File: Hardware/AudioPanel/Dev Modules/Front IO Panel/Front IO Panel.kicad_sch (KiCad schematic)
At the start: 78 parts, among them J101 Screw_Terminal_01x02, J102 2.54mm, J103 JST-PH UART/I2C, J104 2.54mm, U101 AZ1117-5.0, U102 INA219AxDCN, U103 AP3012, U106 NXB0106BQX, U109 QTPy SAMD21, U110 USBLC6-2SC6, U111 USBLC6-2SC6

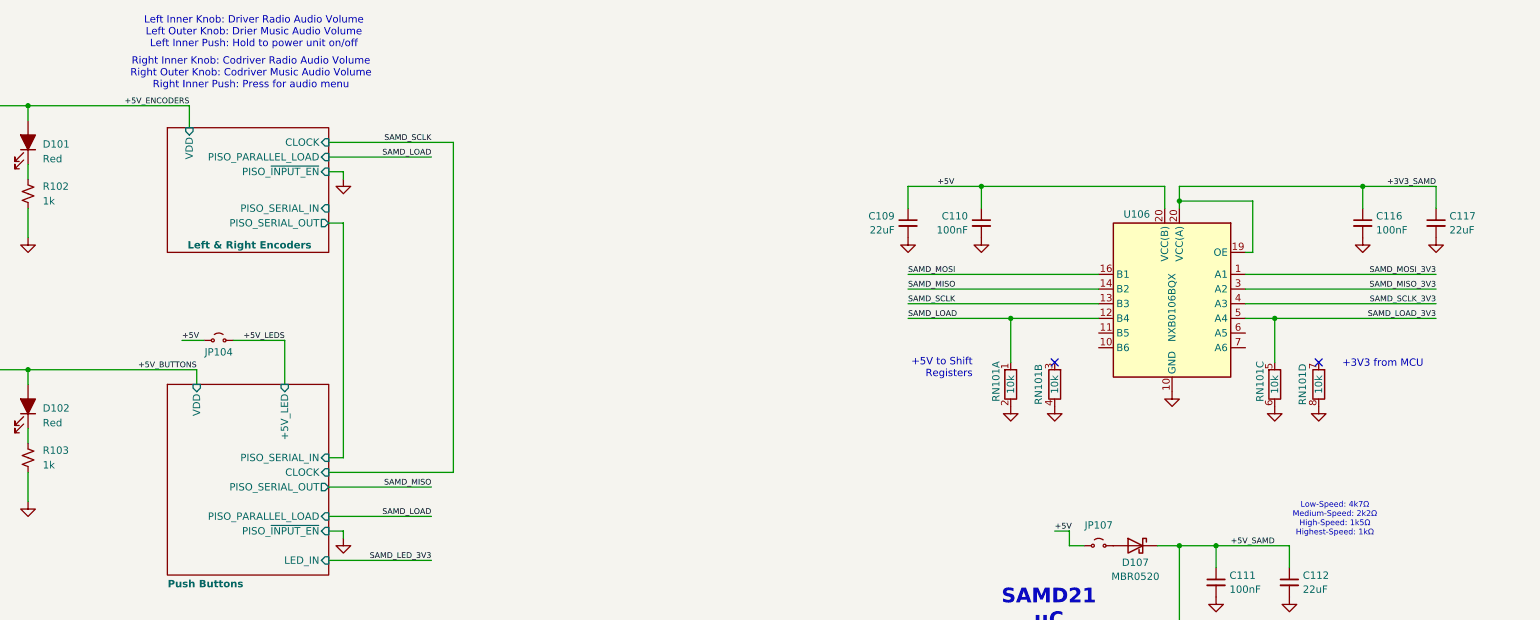
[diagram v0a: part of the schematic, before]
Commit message: Re-organized pull up/dwn resistors in schematic
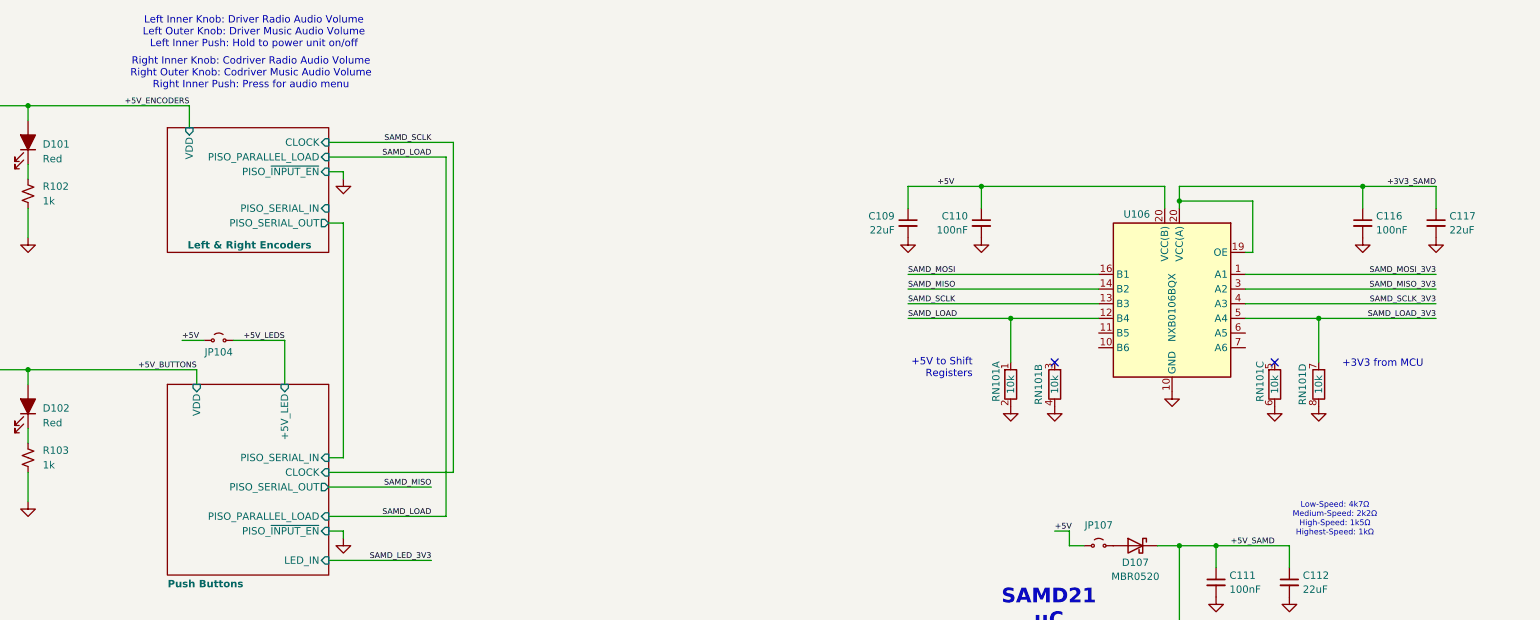
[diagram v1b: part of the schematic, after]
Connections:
- net SAMD_LOAD_3V3: now also RN101.7; no longer RN101.5
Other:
- note added: "Left Inner Knob: Driver Radio Audio Volume Left Outer Knob: Driver Music Audio Volume Left Inner Push: Hold to power unit on/off"
- note removed: "Left Inner Knob: Driver Radio Audio Volume Left Outer Knob: Drier Music Audio Volume Left Inner Push: Hold to power unit on/off"
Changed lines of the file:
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@@
 		)
 	)
-	(text "Left Inner Knob: Driver Radio Audio Volume\nLeft Outer Knob: Drier Music Audio Volume\nLeft Inner Push: Hold to power unit on/off"
+	(text "Left Inner Knob: Driver Radio Audio Volume\nLeft Outer Knob: Driver Music Audio Volume\nLeft Inner Push: Hold to power unit on/off"
 		(exclude_from_sim no)
 		(at 79.756 46.99 0)
@@
 	)
 	(junction
-		(at 256.54 96.52)
-		(diameter 0)
-		(color 0 0 0 0)
-	)
-	(junction
 		(at 242.57 232.41)
 		(diameter 0)
@@
 	)
 	(junction
+		(at 264.16 96.52)
+		(diameter 0)
+		(color 0 0 0 0)
+	)
+	(junction
 		(at 240.03 135.89)
 		(diameter 0)
@@
 	)
 	(no_connect
-		(at 264.16 104.14)
+		(at 256.54 104.14)
 	)
 	(wire
@@
 	(wire
 		(pts
-			(xy 256.54 96.52) (xy 284.48 96.52)
-		)
-		(stroke
-			(width 0)
-			(type default)
-		)
-	)
-	(wire
-		(pts
 			(xy 92.71 173.99) (xy 106.68 173.99)
 		)
@@
 	(wire
 		(pts
-			(xy 251.46 96.52) (xy 256.54 96.52)
+			(xy 251.46 96.52) (xy 264.16 96.52)
 		)
 		(stroke
@@
 	(wire
 		(pts
-			(xy 256.54 96.52) (xy 256.54 104.14)
+			(xy 264.16 96.52) (xy 264.16 104.14)
 		)
 		(stroke
@@
 	(wire
 		(pts
+			(xy 264.16 96.52) (xy 284.48 96.52)
+		)
+		(stroke
+			(width 0)
+			(type default)
+		)
+	)
+	(wire
+		(pts
 			(xy 240.03 135.89) (xy 236.22 135.89)
 		)
@@
 	(wire
 		(pts
-			(xy 92.71 130.81) (xy 110.49 130.81)
+			(xy 92.71 130.81) (xy 113.03 130.81)
 		)
 		(stroke
@@
 	(wire
 		(pts
-			(xy 92.71 68.58) (xy 110.49 68.58)
+			(xy 92.71 68.58) (xy 113.03 68.58)
 		)
 		(stroke
@@
 	(wire
 		(pts
+			(xy 113.03 130.81) (xy 113.03 68.58)
+		)
+		(stroke
+			(width 0)
+			(type default)
+		)
+	)
+	(wire
+		(pts
 			(xy 267.97 243.84) (xy 267.97 232.41)
 		)
@@
 			)
 		)
-		(property "Datasheet" "https://www.ti.com/lit/ds/scas218x/scas218x.pdf"
+		(property "Datasheet" "https://assets.nexperia.com/documents/data-sheet/NXB0106.pdf"
 			(at 240.03 100.33 0)
 			(effects

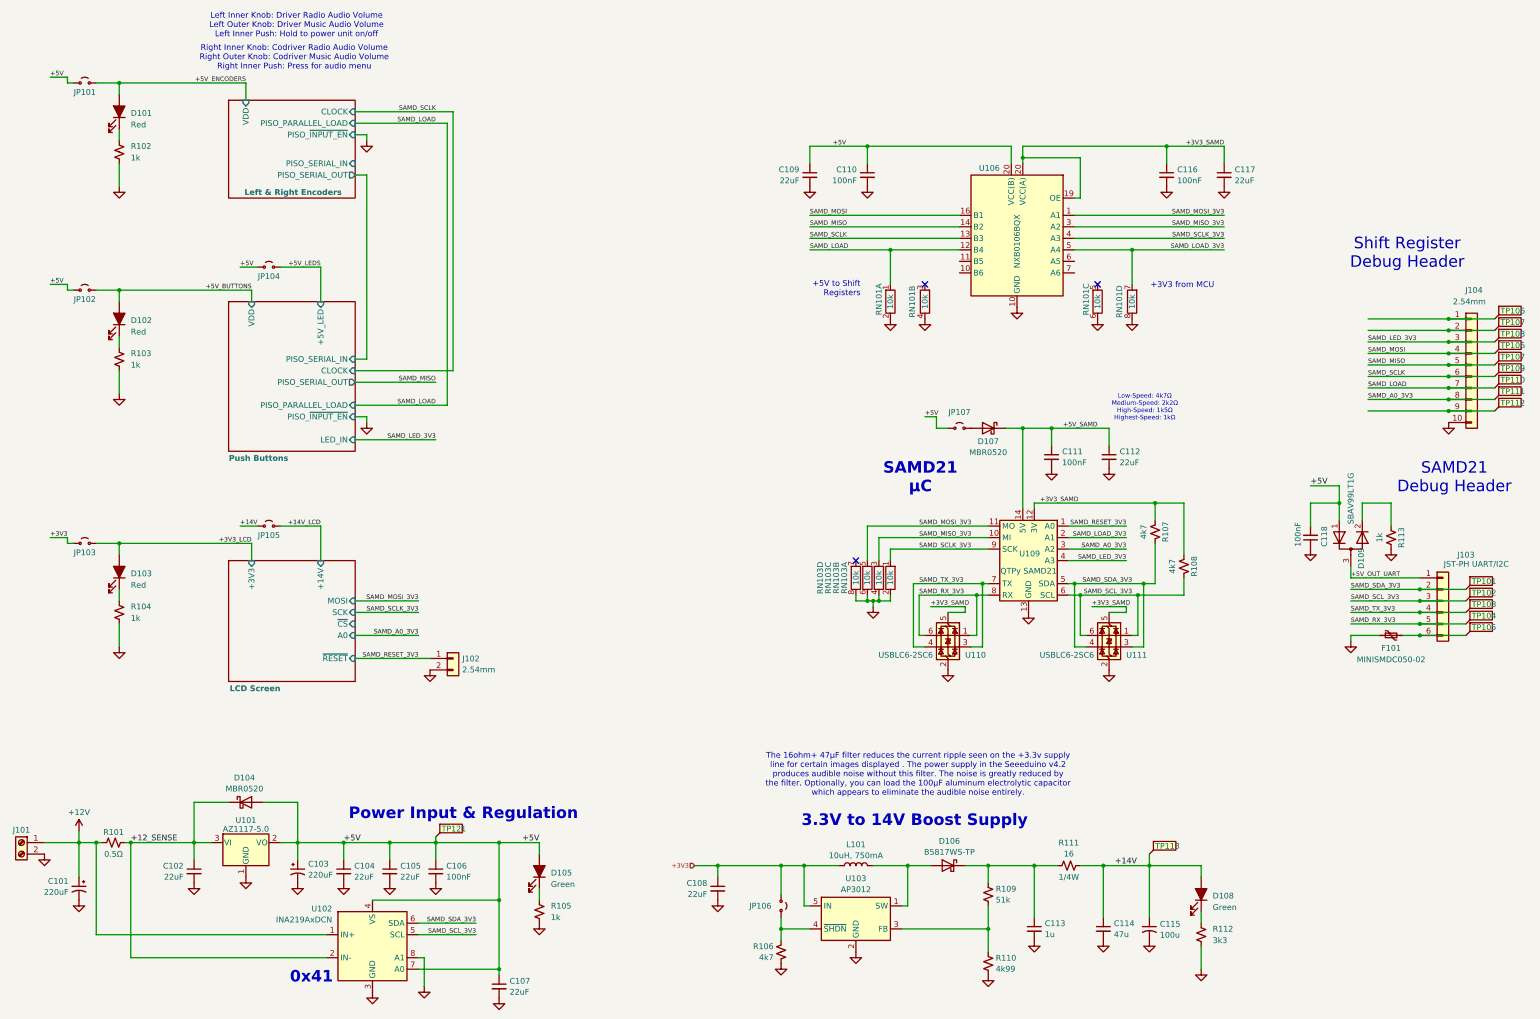
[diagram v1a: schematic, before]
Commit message: Changed encoder, added footprints for buttons
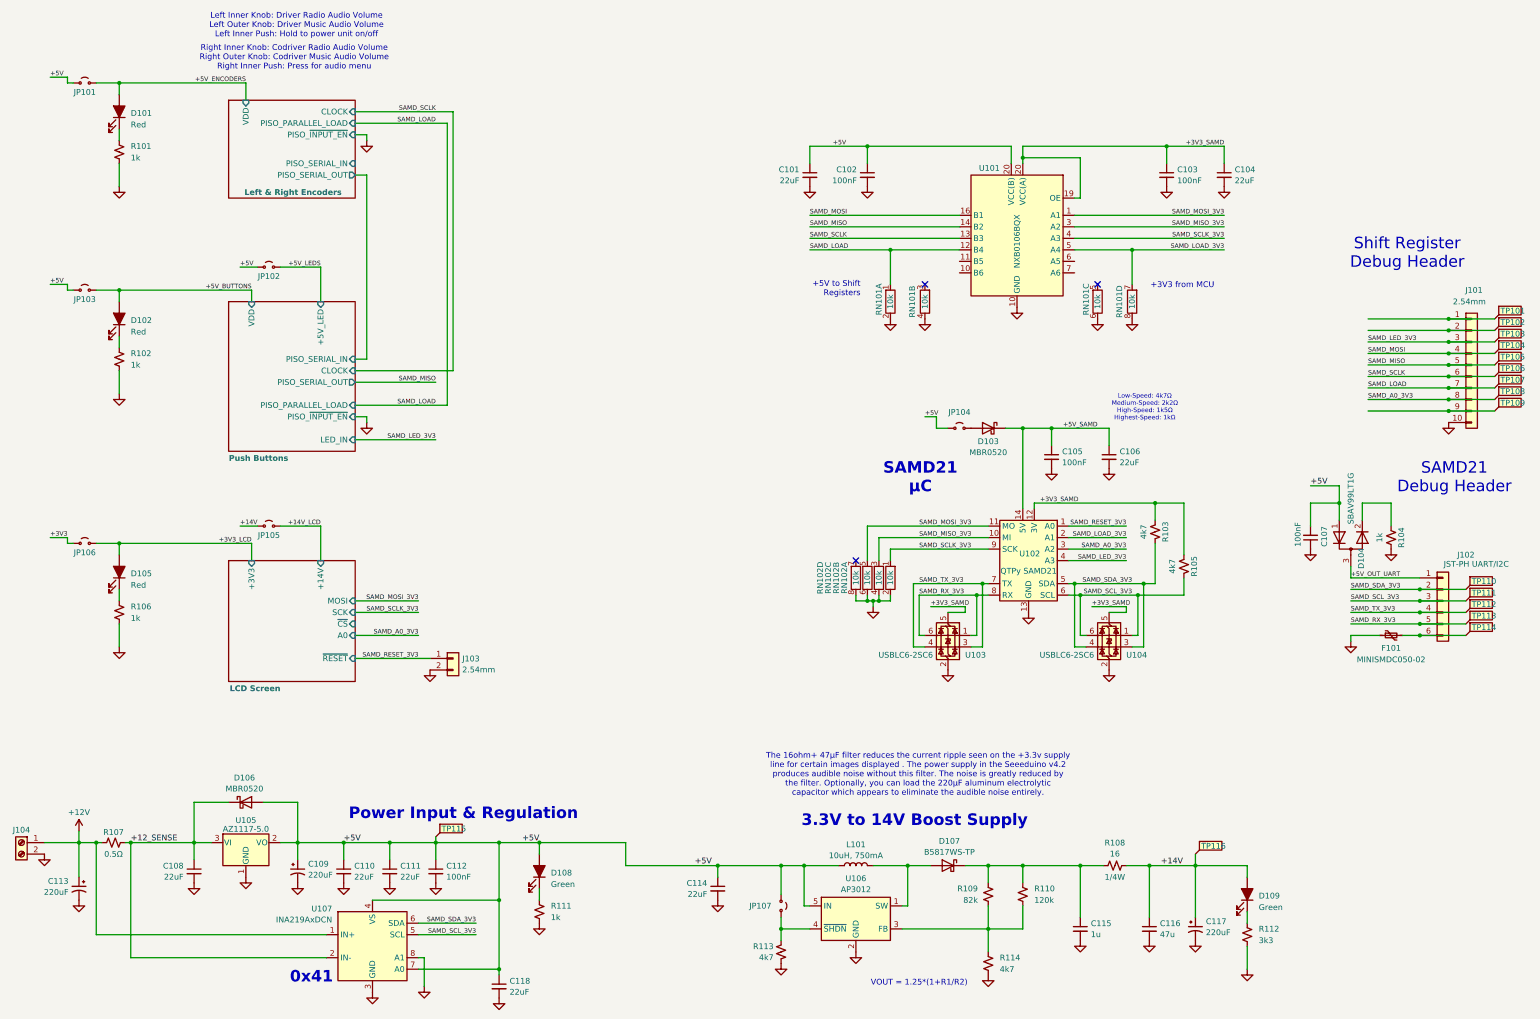
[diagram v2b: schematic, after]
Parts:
- removed C115: 100u, Capacitor_SMD:CP_Elec_6.3x7.7, symbol Device:C_Small_US
- added C117: 220uF, Capacitor_SMD:CP_Elec_6.3x7.7, symbol Device:C_Polarized_Small_US
- added R110: 120k, Libraries:Worthington_R_0402, symbol Device:R_Small_US
- R109: value 51k -> 82k
- R114: renamed from R110; value 4k99 -> 4k7
- renumbered C109 to C101, C110 to C102, C116 to C103, C117 to C104, C111 to C105, C112 to C106, C118 to C107, C102 to C108, C103 to C109, C104 to C110, C105 to C111, C106 to C112, C101 to C113, C108 to C114, C113 to C115, C114 to C116, C107 to C118, D107 to D103, D109 to D104, D103 to D105, D104 to D106, D106 to D107, D105 to D108, D108 to D109, J104 to J101, J103 to J102, J102 to J103, J101 to J104, JP104 to JP102, JP102 to JP103, JP107 to JP104, JP103 to JP106, JP106 to JP107, R102 to R101, R103 to R102, R107 to R103, R113 to R104, R108 to R105, R104 to R106, R101 to R107, R111 to R108, R105 to R111, R106 to R113, RN103 to RN102, TP106 to TP101, TP107 to TP102, TP108 to TP103, TP106 to TP104, TP107 to TP105, TP109 to TP106, TP110 to TP107, TP111 to TP108, TP112 to TP109, TP101 to TP110, TP102 to TP111, TP103 to TP112, TP104 to TP113, TP105 to TP114, TP121 to TP115, TP113 to TP116, U106 to U101, U109 to U102, U110 to U103, U111 to U104, U101 to U105, U103 to U106, U102 to U107
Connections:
- net +14V: now also C117.1
- net +3V3: no longer C114.1, JP107.1 (A), L101.1, U106.5 (IN)
- net +5V: now also C114.1, JP107.1 (A), L101.1, U106.5 (IN)
- net GND: now also C117.2
- net at C115.1, D107.1 (K), R108.1: now also R109.2, R110.1; no longer R109.1
- net at R114.1, U106.3 (FB): now also R109.1, R110.2; no longer R109.2
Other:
- note added: "The 16ohm+ 47µF filter reduces the current ripple seen on the +3.3v supply line for certain images displayed . The power supply in the Seeeduino v4.2 produces audible noise without this filter. The noise is greatly reduced by the filter. Optionally, you can load the 220µF aluminum electrolytic capacitor which appears to eliminate the audible noise entirely."
- note added: "VOUT = 1.25*(1+R1/R2)"
- note removed: "The 16ohm+ 47µF filter reduces the current ripple seen on the +3.3v supply line for certain images displayed . The power supply in the Seeeduino v4.2 produces audible noise without this filter. The noise is greatly reduced by the filter. Optionally, you can load the 100µF aluminum electrolytic capacitor which appears to eliminate the audible noise entirely."
- moved on the sheet: C115, C116, D109, R108, R109, R112, TP116

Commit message: Changed passives to Worthingtons
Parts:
- C105: footprint Capacitor_SMD:C_0402_1005Metric -> Libraries:Worthington_C_0402
- C106: footprint Capacitor_SMD:C_0603_1608Metric -> Libraries:Worthington_C_0603
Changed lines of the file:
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@@
 			)
 		)
-		(property "Footprint" "Capacitor_SMD:C_0402_1005Metric"
+		(property "Footprint" "Libraries:Worthington_C_0402"
 			(at 246.38 142.24 0)
 			(effects
@@
 			)
 		)
-		(property "Footprint" "Capacitor_SMD:C_0603_1608Metric"
+		(property "Footprint" "Libraries:Worthington_C_0603"
 			(at 259.08 142.24 0)
 			(effects

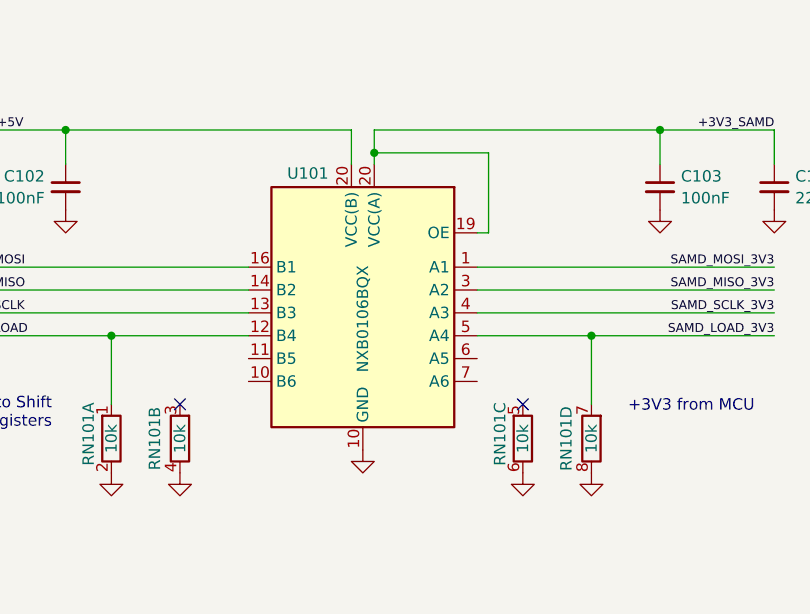
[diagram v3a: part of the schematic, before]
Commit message: Fixed footprint errors, placed onto PCBs
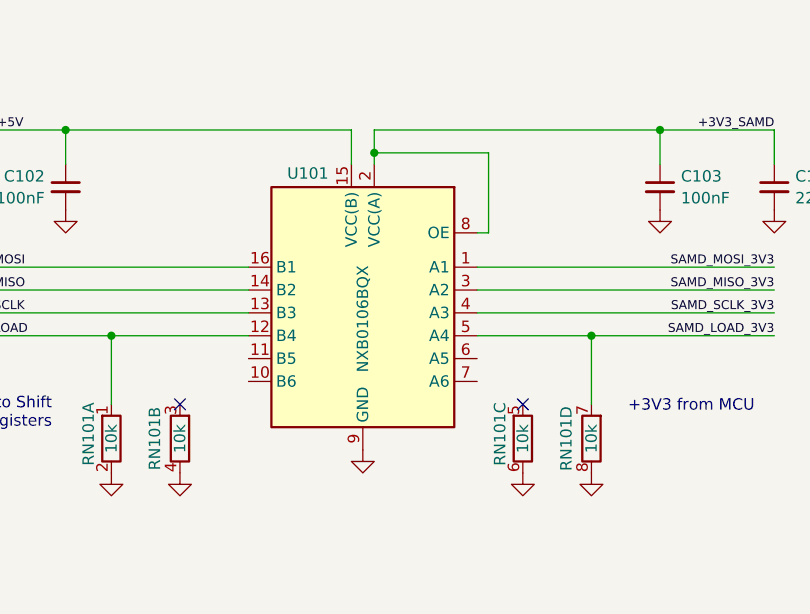
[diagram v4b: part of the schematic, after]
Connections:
- net +3V3_SAMD: now also U101.2 (VCC(A)), U101.8 (OE); no longer U101.19 (OE), U101.20 (VCC(B))
- net +5V: now also U101.15 (VCC(B)); no longer U101.20 (VCC(B))
- net GND: now also U101.17 (GND), U101.9 (GND); no longer U101.10 (B6)
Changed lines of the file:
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@@
-	)
-	(symbol
-		(lib_id "library_symbols:NXB0106BQX")
-		(at 238.76 95.25 0)
-		(mirror y)
-		(unit 1)
-		(exclude_from_sim no)
-		(in_bom yes)
-		(on_board yes)
-		(dnp no)
-		(property "Reference" "U101"
-			(at 234.95 78.486 0)
-			(effects
-				(font
-					(size 1.27 1.27)
-				)
-				(justify left)
-			)
-		)
-		(property "Value" "NXB0106BQX"
-			(at 238.76 100.584 90)
-			(effects
-				(font
-					(size 1.27 1.27)
-				)
-				(justify left)
-			)
-		)
-		(property "Footprint" "Libraries:RGY16_2P55X2P05"
-			(at 215.9 111.76 0)
-			(effects
-				(font
-					(size 1.27 1.27)
-				)
-				(hide yes)
-			)
-		)
-		(property "Datasheet" "https://assets.nexperia.com/documents/data-sheet/NXB0106.pdf"
-			(at 240.03 100.33 0)
-			(effects
-				(font
-					(size 1.27 1.27)
-				)
-				(hide yes)
-			)
-		)
-		(property "Description" "6-Bit Dual supply translating transceiver; auto direction sensing; 3-state"
-			(at 238.76 93.98 0)
-			(effects
-				(font
-					(size 1.27 1.27)
-				)
-				(hide yes)
-			)
-		)
-		(pin "1"
-		)
-		(pin "10"
-		)
-		(pin "11"
-		)
-		(pin "20"
-		)
-		(pin "14"
-		)
-		(pin "5"
-		)
-		(pin "10"
-		)
-		(pin "6"
-		)
-		(pin "16"
-		)
-		(pin "20"
-		)
-		(pin "13"
-		)
-		(pin "3"
-		)
-		(pin "7"
-		)
-		(pin "4"
-		)
-		(pin "19"
-		)
-		(pin "12"
-		)
-		(instances
-			(project "Front IO Panel"
-				(path "/5115d310-a9f7-4cd2-bb07-2c33745c004f"
-					(reference "U101")
-					(unit 1)
-				)
-			)
-		)
 	)
 	(symbol
@@
 					(unit 1)
 				)
+			)
+		)
+	)
+	(symbol
+		(lib_id "library_symbols:NXB0106BQX")
+		(at 238.76 95.25 0)
+		(mirror y)
+		(unit 1)
+		(exclude_from_sim no)
+		(in_bom yes)
+		(on_board yes)
+		(dnp no)
+		(property "Reference" "U101"
+			(at 234.95 78.486 0)
+			(effects
+				(font
+					(size 1.27 1.27)
+				)
+				(justify left)
+			)
+		)
+		(property "Value" "NXB0106BQX"
+			(at 238.76 100.584 90)
+			(effects
+				(font
+					(size 1.27 1.27)
+				)
+				(justify left)
+			)
+		)
+		(property "Footprint" "Libraries:RGY16_2P55X2P05"
+			(at 215.9 111.76 0)
+			(effects
+				(font
+					(size 1.27 1.27)
+				)
+				(hide yes)
+			)
+		)
+		(property "Datasheet" "https://www.ti.com/lit/ds/scas218x/scas218x.pdf"
+			(at 240.03 100.33 0)
+			(effects
+				(font
+					(size 1.27 1.27)
+				)
+				(hide yes)
+			)
+		)
+		(property "Description" "6-Bit Dual supply translating transceiver; auto direction sensing; 3-state"
+			(at 238.76 93.98 0)
+			(effects
+				(font
+					(size 1.27 1.27)
+				)
+				(hide yes)
+			)
+		)
+		(pin "17"
+		)
+		(pin "10"
+		)
+		(pin "11"
+		)
+		(pin "2"
+		)
+		(pin "14"
+		)
+		(pin "5"
+		)
+		(pin "9"
+		)
+		(pin "6"
+		)
+		(pin "16"
+		)
+		(pin "8"
+		)
+		(pin "13"
+		)
+		(pin "3"
+		)
+		(pin "7"
+		)
+		(pin "4"
+		)
+		(pin "15"
+		)
+		(pin "12"
+		)
+		(pin "1"
+		)
+		(instances
+			(project "Front IO Panel"
+				(path "/5115d310-a9f7-4cd2-bb07-2c33745c004f"
+					(reference "U101")
+					(unit 1)
+				)
